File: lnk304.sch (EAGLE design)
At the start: 19 parts, among them IC1 TPS774, IC2 MCP1703CB

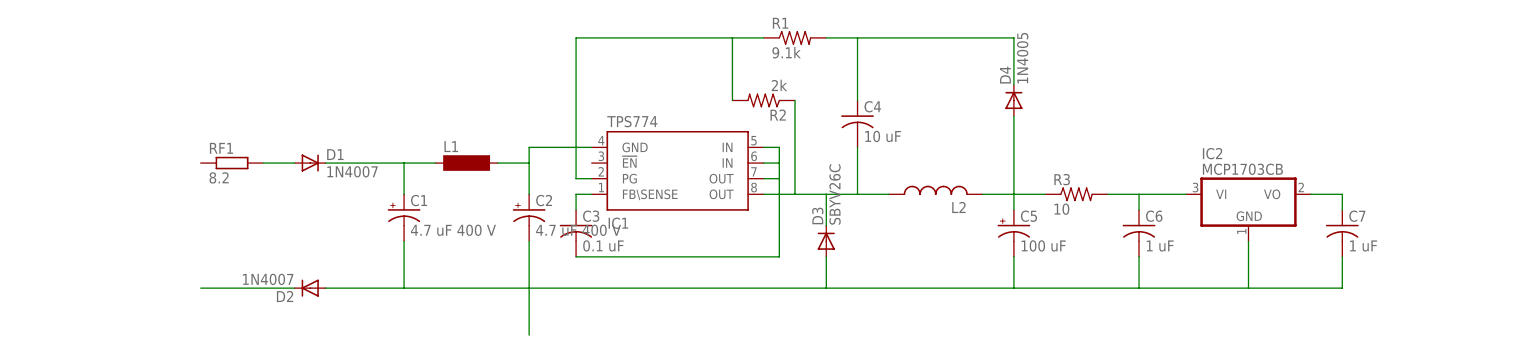
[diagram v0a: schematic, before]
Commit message: Redesign to add Controller above the converter using pin headers
** 19.Mar.2016 **
Schematic:
- Change RF1 to fuse component
- Added Controller pin headers

PCB Layout:
- Increase board length from 46mm to 49.5mm
- Re orientation of components
RF1, D1, C1, C2, L2 R3 are the main components which were moved for long
distance
- Added Common Plane for Source pin of LNK

-- Missing --
- Need to revise Terminal Block size and overlapping with D2
- The LNK layout used till now is not the correct one.
- May need to increase L2 pad distance a bit
- May need to decrease the board height by 2mm

NOTE: Till now the design is just a fast draft. You can see that some
traces are not drawn in a clean way.
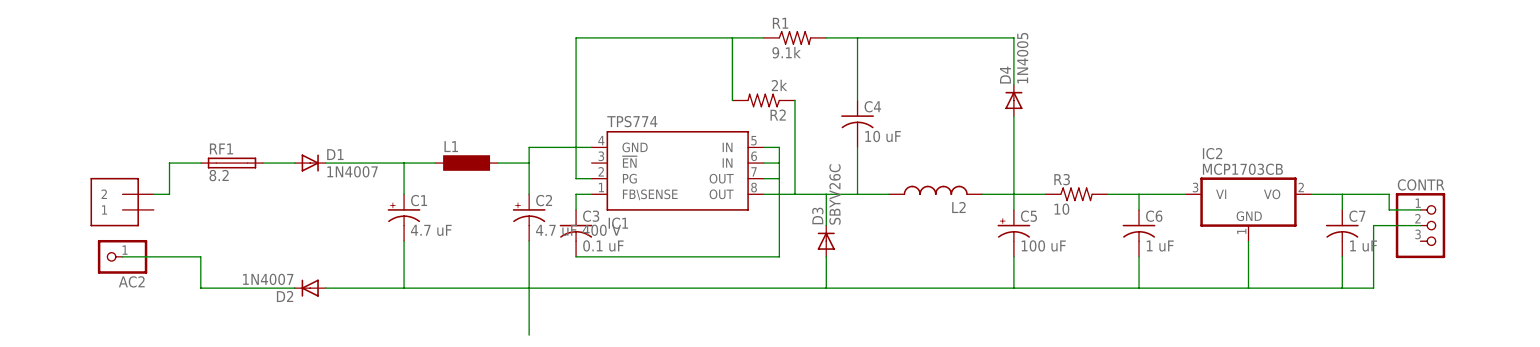
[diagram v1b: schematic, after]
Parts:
- added AC: 1X2-3.5MM, adafruit:1X2-3.5MM
- added AC2: (no value), adafruit:PINHD-1X1
- added CONTR: (no value), adafruit:PINHD-1X3
- C1: value 4.7 uF 400 V -> 4.7 uF
- RF1: device resistor:R-EU_0204/7 -> fuse:FUSEPICOFUSE
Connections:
- new net N$9: AC.2, RF1.1
- net GND: now also CONTR.2
- net N$14: now also CONTR.1
- net N$6: now also AC2.1
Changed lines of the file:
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@@
 <grid distance="0.1" unitdist="inch" unit="inch" style="lines" multiple="1" display="no" altdistance="0.01" altunitdist="inch" altunit="inch"/>
 <layers>
-<layer number="1" name="Top" color="4" fill="1" visible="yes" active="no"/>
-<layer number="16" name="Bottom" color="1" fill="1" visible="yes" active="no"/>
-<layer number="17" name="Pads" color="2" fill="1" visible="yes" active="no"/>
-<layer number="18" name="Vias" color="2" fill="1" visible="yes" active="no"/>
-<layer number="19" name="Unrouted" color="6" fill="1" visible="yes" active="no"/>
-<layer number="20" name="Dimension" color="15" fill="1" visible="yes" active="no"/>
-<layer number="21" name="tPlace" color="7" fill="1" visible="yes" active="no"/>
-<layer number="22" name="bPlace" color="7" fill="1" visible="yes" active="no"/>
-<layer number="23" name="tOrigins" color="15" fill="1" visible="yes" active="no"/>
-<layer number="24" name="bOrigins" color="15" fill="1" visible="yes" active="no"/>
-<layer number="25" name="tNames" color="7" fill="1" visible="yes" active="no"/>
-<layer number="26" name="bNames" color="7" fill="1" visible="yes" active="no"/>
-<layer number="27" name="tValues" color="7" fill="1" visible="yes" active="no"/>
-<layer number="28" name="bValues" color="7" fill="1" visible="yes" active="no"/>
+<layer number="1" name="Top" color="4" fill="1" visible="no" active="no"/>
+<layer number="16" name="Bottom" color="1" fill="1" visible="no" active="no"/>
+<layer number="17" name="Pads" color="2" fill="1" visible="no" active="no"/>
+<layer number="18" name="Vias" color="2" fill="1" visible="no" active="no"/>
+<layer number="19" name="Unrouted" color="6" fill="1" visible="no" active="no"/>
+<layer number="20" name="Dimension" color="15" fill="1" visible="no" active="no"/>
+<layer number="21" name="tPlace" color="7" fill="1" visible="no" active="no"/>
+<layer number="22" name="bPlace" color="7" fill="1" visible="no" active="no"/>
+<layer number="23" name="tOrigins" color="15" fill="1" visible="no" active="no"/>
+<layer number="24" name="bOrigins" color="15" fill="1" visible="no" active="no"/>
+<layer number="25" name="tNames" color="7" fill="1" visible="no" active="no"/>
+<layer number="26" name="bNames" color="7" fill="1" visible="no" active="no"/>
+<layer number="27" name="tValues" color="7" fill="1" visible="no" active="no"/>
+<layer number="28" name="bValues" color="7" fill="1" visible="no" active="no"/>
 <layer number="29" name="tStop" color="7" fill="3" visible="no" active="no"/>
 <layer number="30" name="bStop" color="7" fill="6" visible="no" active="no"/>
@@
 <layer number="35" name="tGlue" color="7" fill="4" visible="no" active="no"/>
 <layer number="36" name="bGlue" color="7" fill="5" visible="no" active="no"/>
-<layer number="37" name="tTest" color="7" fill="1" visible="yes" active="no"/>
-<layer number="38" name="bTest" color="7" fill="1" visible="yes" active="no"/>
+<layer number="37" name="tTest" color="7" fill="1" visible="no" active="no"/>
+<layer number="38" name="bTest" color="7" fill="1" visible="no" active="no"/>
 <layer number="39" name="tKeepout" color="4" fill="11" visible="no" active="no"/>
 <layer number="40" name="bKeepout" color="1" fill="11" visible="no" active="no"/>
@@
 <layer number="44" name="Drills" color="7" fill="1" visible="no" active="no"/>
 <layer number="45" name="Holes" color="7" fill="1" visible="no" active="no"/>
-<layer number="46" name="Milling" color="3" fill="1" visible="yes" active="no"/>
-<layer number="47" name="Measures" color="7" fill="1" visible="yes" active="no"/>
-<layer number="48" name="Document" color="7" fill="1" visible="yes" active="no"/>
-<layer number="49" name="Reference" color="7" fill="1" visible="yes" active="no"/>
-<layer number="50" name="dxf" color="7" fill="1" visible="yes" active="no"/>
-<layer number="51" name="tDocu" color="7" fill="1" visible="yes" active="no"/>
-<layer number="52" name="bDocu" color="7" fill="1" visible="yes" active="no"/>
-<layer number="53" name="tGND_GNDA" color="7" fill="9" visible="yes" active="no"/>
-<layer number="54" name="bGND_GNDA" color="1" fill="9" visible="yes" active="no"/>
-<layer number="56" name="wert" color="7" fill="1" visible="yes" active="no"/>
-<layer number="57" name="tCAD" color="7" fill="1" visible="yes" active="no"/>
+<layer number="46" name="Milling" color="3" fill="1" visible="no" active="no"/>
+<layer number="47" name="Measures" color="7" fill="1" visible="no" active="no"/>
+<layer number="48" name="Document" color="7" fill="1" visible="no" active="no"/>
+<layer number="49" name="Reference" color="7" fill="1" visible="no" active="no"/>
+<layer number="50" name="dxf" color="7" fill="1" visible="no" active="no"/>
+<layer number="51" name="tDocu" color="7" fill="1" visible="no" active="no"/>
+<layer number="52" name="bDocu" color="7" fill="1" visible="no" active="no"/>
+<layer number="53" name="tGND_GNDA" color="7" fill="9" visible="no" active="no"/>
+<layer number="54" name="bGND_GNDA" color="1" fill="9" visible="no" active="no"/>
+<layer number="56" name="wert" color="7" fill="1" visible="no" active="no"/>
+<layer number="57" name="tCAD" color="7" fill="1" visible="no" active="no"/>
 <layer number="90" name="Modules" color="5" fill="1" visible="yes" active="yes"/>
 <layer number="91" name="Nets" color="2" fill="1" visible="yes" active="yes"/>
@@
 </classes>
 <parts>
-<part name="RF1" library="resistor" deviceset="R-EU_" device="0204/7" value="8.2"/>
+<part name="RF1" library="fuse" deviceset="FUSE" device="PICOFUSE" value="8.2"/>
 <part name="D1" library="adafruit" deviceset="1N4004" device="" value="1N4007"/>
 <part name="D2" library="adafruit" deviceset="1N4004" device="" value="1N4007"/>
-<part name="C1" library="adafruit" deviceset="CPOL-US" device="E5-10.5" value="4.7 uF 400 V"/>
+<part name="C1" library="adafruit" deviceset="CPOL-US" device="E5-10.5" value="4.7 uF"/>
 <part name="C2" library="adafruit" deviceset="CPOL-US" device="E5-10.5" value="4.7 uF 400 V"/>
 <part name="L1" library="inductor-neosid" deviceset="BS" device="11"/>
@@
 <part name="C6" library="adafruit" deviceset="C-US" device="C0603" value="1 uF"/>
 <part name="C7" library="adafruit" deviceset="C-US" device="C0603" value="1 uF"/>
+<part name="AC" library="adafruit" deviceset="1X2" device="-3.5MM"/>
+<part name="AC2" library="adafruit" deviceset="PINHD-1X1" device=""/>
+<part name="CONTR" library="adafruit" deviceset="PINHD-1X3" device=""/>
 </parts>
 <sheets>
@@
 <instance part="C6" gate="G$1" x="152.4" y="50.8"/>
 <instance part="C7" gate="G$1" x="185.42" y="50.8"/>
+<instance part="AC" gate="G$1" x="-12.7" y="55.88" rot="R180"/>
+<instance part="AC2" gate="G$1" x="-15.24" y="45.72" rot="R180"/>
+<instance part="CONTR" gate="A" x="200.66" y="50.8"/>
 </instances>
 <busses>
@@
 <pinref part="D2" gate="1" pin="C"/>
 <wire x1="15.24" y1="40.64" x2="0" y2="40.64" width="0.1524" layer="91"/>
+<pinref part="AC2" gate="G$1" pin="1"/>
+<wire x1="-12.7" y1="45.72" x2="0" y2="45.72" width="0.1524" layer="91"/>
+<wire x1="0" y1="45.72" x2="0" y2="40.64" width="0.1524" layer="91"/>
 </segment>
 </net>
@@
 <wire x1="170.18" y1="48.26" x2="170.18" y2="40.64" width="0.1524" layer="91"/>
 <wire x1="53.34" y1="40.64" x2="53.34" y2="33.02" width="0.1524" layer="91"/>
+<pinref part="CONTR" gate="A" pin="2"/>
+<wire x1="198.12" y1="50.8" x2="190.5" y2="50.8" width="0.1524" layer="91"/>
+<wire x1="190.5" y1="50.8" x2="190.5" y2="40.64" width="0.1524" layer="91"/>
+<wire x1="190.5" y1="40.64" x2="185.42" y2="40.64" width="0.1524" layer="91"/>
 </segment>
 </net>
@@
 <pinref part="IC2" gate="G$1" pin="VO"/>
 <wire x1="185.42" y1="55.88" x2="180.34" y2="55.88" width="0.1524" layer="91"/>
-</segment>
-</net>
+<wire x1="185.42" y1="55.88" x2="193.04" y2="55.88" width="0.1524" layer="91"/>
+<wire x1="193.04" y1="55.88" x2="193.04" y2="53.34" width="0.1524" layer="91"/>
+<pinref part="CONTR" gate="A" pin="1"/>
+<wire x1="193.04" y1="53.34" x2="198.12" y2="53.34" width="0.1524" layer="91"/>
+</segment>
+</net>
+<net name="N$9" class="0">
+<segment>
+<pinref part="AC" gate="G$1" pin="2"/>
+<wire x1="-7.62" y1="55.88" x2="-5.08" y2="55.88" width="0.1524" layer="91"/>
+<wire x1="-5.08" y1="55.88" x2="-5.08" y2="60.96" width="0.1524" layer="91"/>
+<pinref part="RF1" gate="G$1" pin="1"/>
+<wire x1="-5.08" y1="60.96" x2="0" y2="60.96" width="0.1524" layer="91"/>
+</segment>
+</net>

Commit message: Added 9v output pins
** 21.Mar.2016 **
Schematic:
- Added pin headers for 9v output which will be used by the relays
- Added extra ground pin to CONTR component

PCB Layout:
- Added pin headers for 9v output which will be used by the relays
- Added extra ground pin to CONTR component
- Added two 1mm holes
- Added Ground plane

Missing:
- Same issues
- Add Creepage between C1 and C2 pads
- Smash right side components and re organise the components names on
the silk screen
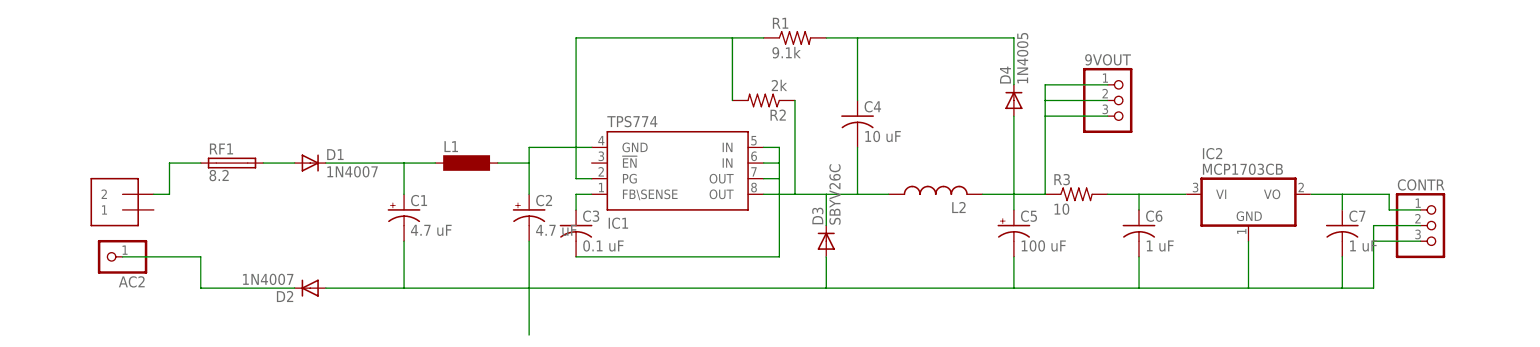
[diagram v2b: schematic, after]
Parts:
- added 9VOUT: (no value), adafruit:PINHD-1X3
- C2: value 4.7 uF 400 V -> 4.7 uF
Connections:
- net GND: now also CONTR.3
- net N$4: now also 9VOUT.1, 9VOUT.2, 9VOUT.3
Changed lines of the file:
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@@
 <part name="D2" library="adafruit" deviceset="1N4004" device="" value="1N4007"/>
 <part name="C1" library="adafruit" deviceset="CPOL-US" device="E5-10.5" value="4.7 uF"/>
-<part name="C2" library="adafruit" deviceset="CPOL-US" device="E5-10.5" value="4.7 uF 400 V"/>
+<part name="C2" library="adafruit" deviceset="CPOL-US" device="E5-10.5" value="4.7 uF"/>
 <part name="L1" library="inductor-neosid" deviceset="BS" device="11"/>
 <part name="C4" library="adafruit" deviceset="C-US" device="C0603" value="10 uF"/>
@@
 <part name="AC2" library="adafruit" deviceset="PINHD-1X1" device=""/>
 <part name="CONTR" library="adafruit" deviceset="PINHD-1X3" device=""/>
+<part name="9VOUT" library="adafruit" deviceset="PINHD-1X3" device=""/>
 </parts>
 <sheets>
@@
 <instance part="AC2" gate="G$1" x="-15.24" y="45.72" rot="R180"/>
 <instance part="CONTR" gate="A" x="200.66" y="50.8"/>
+<instance part="9VOUT" gate="A" x="149.86" y="71.12"/>
 </instances>
 <busses>
@@
 <pinref part="CONTR" gate="A" pin="2"/>
 <wire x1="198.12" y1="50.8" x2="190.5" y2="50.8" width="0.1524" layer="91"/>
-<wire x1="190.5" y1="50.8" x2="190.5" y2="40.64" width="0.1524" layer="91"/>
+<wire x1="190.5" y1="50.8" x2="190.5" y2="48.26" width="0.1524" layer="91"/>
+<wire x1="190.5" y1="48.26" x2="190.5" y2="40.64" width="0.1524" layer="91"/>
 <wire x1="190.5" y1="40.64" x2="185.42" y2="40.64" width="0.1524" layer="91"/>
+<pinref part="CONTR" gate="A" pin="3"/>
+<wire x1="198.12" y1="48.26" x2="190.5" y2="48.26" width="0.1524" layer="91"/>
 </segment>
 </net>
@@
 <wire x1="132.08" y1="55.88" x2="132.08" y2="68.58" width="0.1524" layer="91"/>
 <pinref part="R3" gate="G$1" pin="1"/>
-<wire x1="137.16" y1="55.88" x2="132.08" y2="55.88" width="0.1524" layer="91"/>
+<wire x1="132.08" y1="55.88" x2="137.16" y2="55.88" width="0.1524" layer="91"/>
+<wire x1="137.16" y1="55.88" x2="137.16" y2="68.58" width="0.1524" layer="91"/>
+<pinref part="9VOUT" gate="A" pin="1"/>
+<wire x1="137.16" y1="68.58" x2="137.16" y2="71.12" width="0.1524" layer="91"/>
+<wire x1="137.16" y1="71.12" x2="137.16" y2="73.66" width="0.1524" layer="91"/>
+<wire x1="137.16" y1="73.66" x2="147.32" y2="73.66" width="0.1524" layer="91"/>
+<pinref part="9VOUT" gate="A" pin="2"/>
+<wire x1="137.16" y1="71.12" x2="147.32" y2="71.12" width="0.1524" layer="91"/>
+<pinref part="9VOUT" gate="A" pin="3"/>
+<wire x1="137.16" y1="68.58" x2="147.32" y2="68.58" width="0.1524" layer="91"/>
 </segment>
 </net>

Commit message: Added the new package LNK30X
** 26.Mar.2016 **
- Checked in new file userdefined.lbr
- Created new device LNK30X
- The device has Symbol name LNK30X
- The device has Package name SO08C

Schematic:
- Added the new package LNK30X and rename component to LNK304

PCB Layout:
- Route the new package LNK30X
- Smash right side components and re organise the components names on
the silk screen
- Added two holes

-- Missing --
- Need to add hot and neutral pins for AC plug concept
- Need to revise Terminal Block size and overlapping with D2
- May need to increase L2 pad distance a bit
- May need to decrease the board height by 2mm
- Add Creepage between C1 and C2 pads
- Revise the two holes diameter and availability of screws
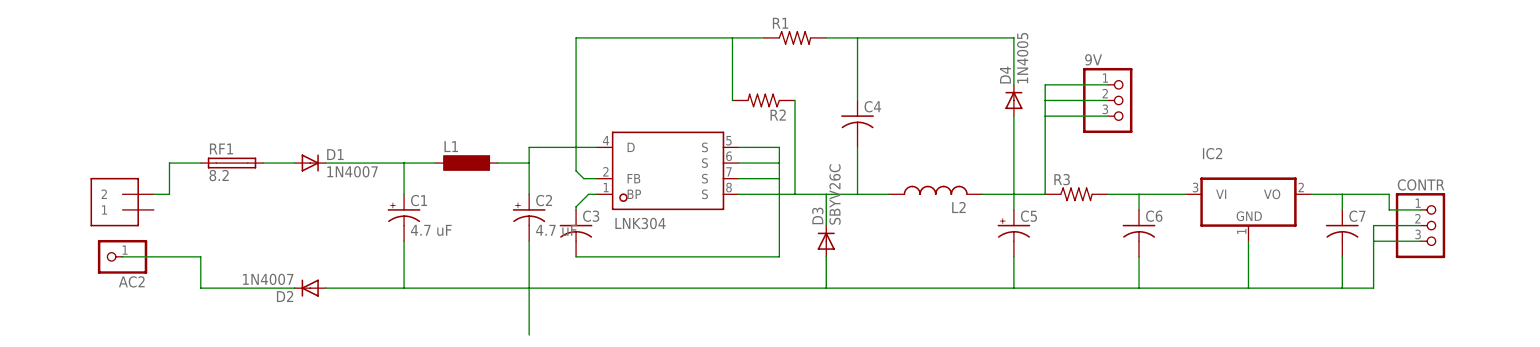
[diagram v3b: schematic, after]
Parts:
- removed IC1: TPS774, texas:TPS774
- added LNK304: LNK30X, userdefined:LNK30X
- C3: value 0.1 uF -> (none)
- C4: value 10 uF -> (none)
- C5: value 100 uF -> (none)
- C6, C7: value 1 uF -> (none)
- R1: value 9.1k -> (none)
- R2: value 2k -> (none)
- R3: value 10 -> (none)
- renumbered 9VOUT to 9V
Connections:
- net N$3: now also LNK304.D; no longer IC1.GND
- net N$5: now also LNK304.FB; no longer IC1.PG
- net N$7: now also LNK304.BP; no longer IC1.FB\SENSE
- net N$8: now also LNK304.S@1, LNK304.S@2, LNK304.S@3, LNK304.S@4; no longer IC1.IN@1, IC1.IN@2, IC1.OUT@1, IC1.OUT@2

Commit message: Added Bleeder resistor and varistor
** 26.Mar.2016 **
Schematic:
- Added a 1M 1/4Watt beelding resistor between hot and neutral
- Added Varistor VR1

PCB Layout:
- Change board height to 49.5mm
- Change trace width to 40mil
- Added a 1M 1/4Watt beelding resistor between hot and neutral
- Change layout of D2 to be shorter so that AC Terminal Block can fit
- Added Varistor VR1

-- Missing --
- Need to add hot and neutral pins for AC plug concept
- Need to revise Terminal Block size and overlapping with D2
- May need to increase L2 pad distance a bit
- May need to decrease the board height by 2mm
- Add Creepage between C1 and C2 pads
- Revise the two holes diameter and availability of screws

-- What can be changed --
- Hot and Neutral pins can be in one signale TBlock02 not 03
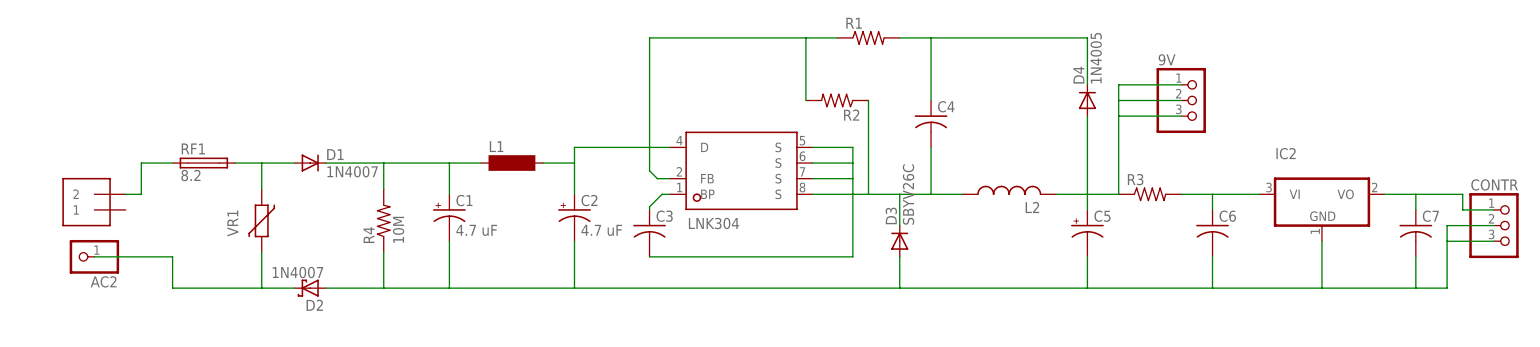
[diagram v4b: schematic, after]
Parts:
- added R4: 10M, resistor:R-US_R1206
- added VR1: VARISTOR-7,5, varistor:VARISTOR-7,5
- D2: device adafruit:1N4004 -> adafruit:SCHOTTKY-DIODEDO41-7
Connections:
- net GND: now also R4.1
- net N$1: now also VR1.1
- net N$2: now also R4.2
- net N$6: now also VR1.2
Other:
- moved on the sheet: 9V, AC2, C1, C2, C3, C4, C5, C6, C7, CONTR, D3, D4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
